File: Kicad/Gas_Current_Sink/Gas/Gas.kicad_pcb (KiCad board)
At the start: 2 copper layers, 135 x 75 mm, 31 parts, among them J1 MG811, J2 Digital, J3 MQ135, J4 CCS811, J5 Analog, J6 CONN_01X02, J7 CONN_01X02

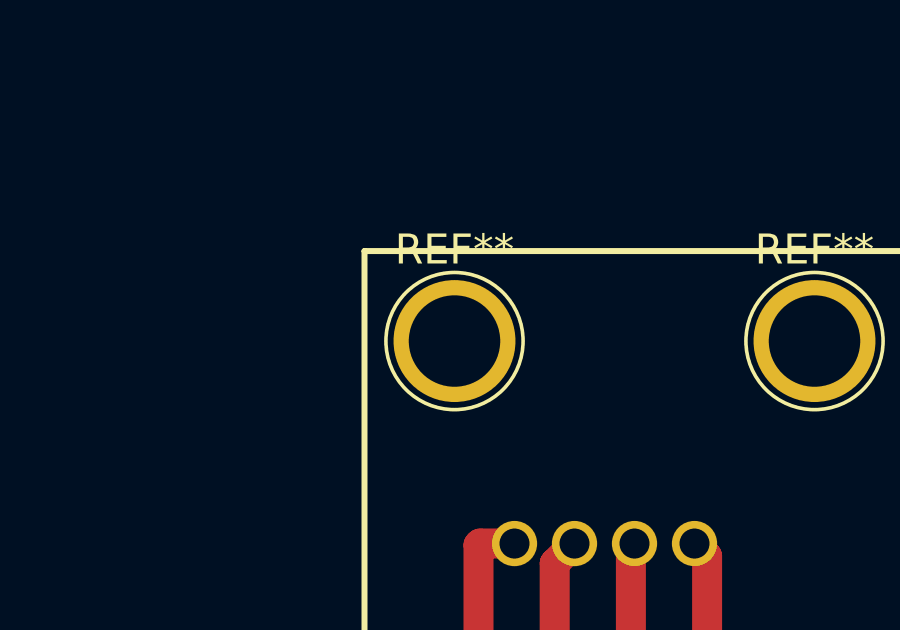
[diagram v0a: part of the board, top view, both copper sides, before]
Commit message: CO2 & Current Arduino final release with necessary calibrations. Minor file structure changes.
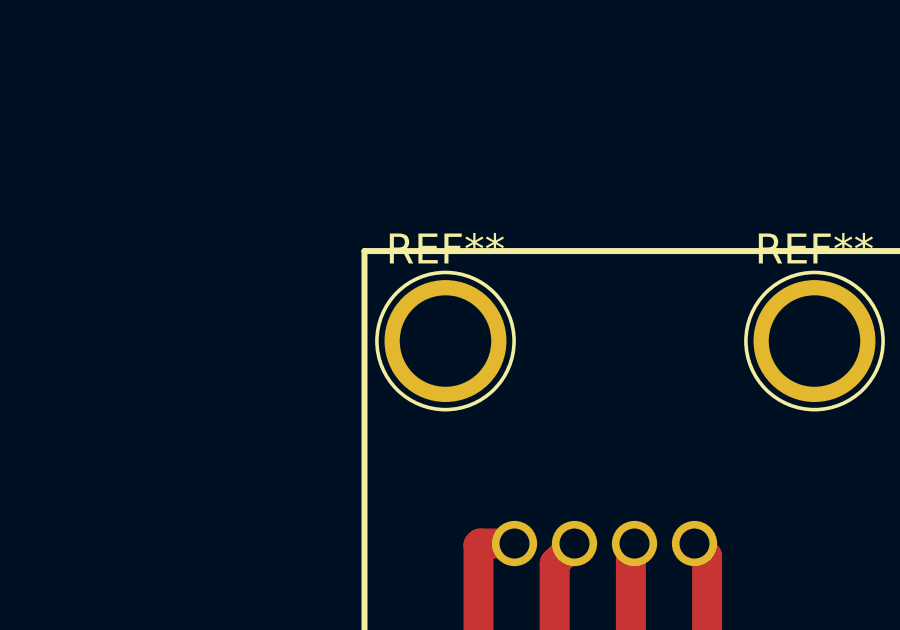
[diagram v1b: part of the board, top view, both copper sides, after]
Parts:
- moved REF** 0.30 mm to (87.7, 114.5)
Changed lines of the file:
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@@
     (links 27)
     (no_connects 0)
-    (area 67.924999 70.924999 203.075001 146.075001)
+    (area 44.650001 70.899999 217.85 156.700001)
     (thickness 1.6)
     (drawings 28)
@@
     (pad 1 thru_hole circle (at 0 0) (size 4.064 4.064) (drill 3.048) (layers *.Cu *.Mask))
   )
-  (module Connectors:1pin locked (layer F.Cu)
-    (at 88 114.5)
+  (module Connectors:1pin (layer F.Cu)
+    (at 87.7 114.5)
     (descr "module 1 pin (ou trou mecanique de percage)")
     (tags DEV)
